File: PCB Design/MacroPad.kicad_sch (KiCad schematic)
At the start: 64 parts, among them J1 USB_C_Receptacle_USB2.0_16P, J2 Conn_01x03_Pin, SW1 SW_DPST, SW2 SW_DPST, U1 RP2040, U2 AMS1117-3.3, U3 W25Q128JVS, U4 SN74LV1T34DBV, Y1 ABM8-272-T3

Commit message: Add second sheet
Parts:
- added C25: 1uF, symbol Device:C_Small
- added R25: 100M, symbol Device:R_Small
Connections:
- net +5V: now also R25.1
- net GND: now also C25.1
- new net +5V_LED: C25.2, R25.2
- no-connect marks 4 -> 12
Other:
- added sheet Keys (MCU_&_Power.kicad_sch)
- note added: "RESET"
- note removed: "RESET BUTTON"
- moved on the sheet: C23, D5, D6, D7, R16, R17, R18, R19, R20, U4

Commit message: Refactor and layout page 1
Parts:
- C23: value C_Small -> 100nF
- U4: value SN74LV1T34DBV -> SN74LV1T34DBVR
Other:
- note added: "LED SIGNAL LEVEL SHIFTER"
- note added: "POWER FOR KEY LEDS"
- note removed: "LED LEVEL SHIFTER"
- moved on the sheet: C1, C10, C11, C12, C13, C14, C15, C16, C17, C18, C19, C2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

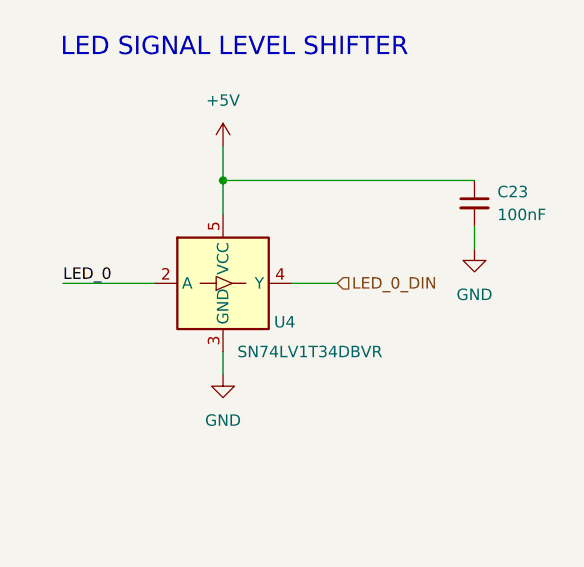
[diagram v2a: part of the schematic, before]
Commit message: Add underkey LEDs to schematic
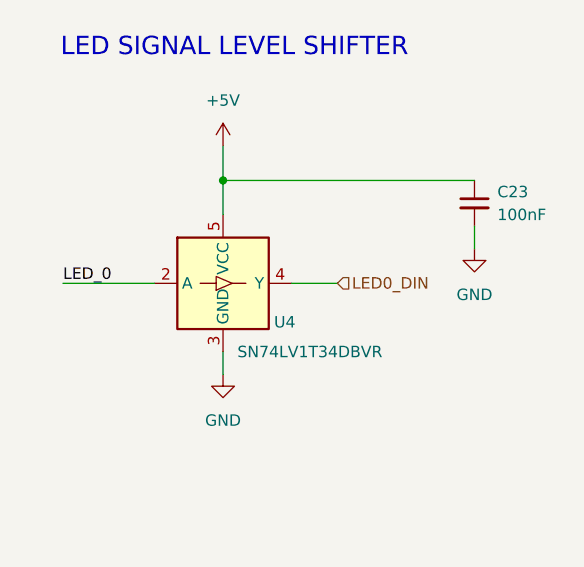
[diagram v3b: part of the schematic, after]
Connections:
- net LED_0_DIN renamed LED0_DIN
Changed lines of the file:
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@@
 		)
 	)
-	(hierarchical_label "LED_0_DIN"
+	(hierarchical_label "LED0_DIN"
 		(shape input)
 		(at 377.19 109.22 0)

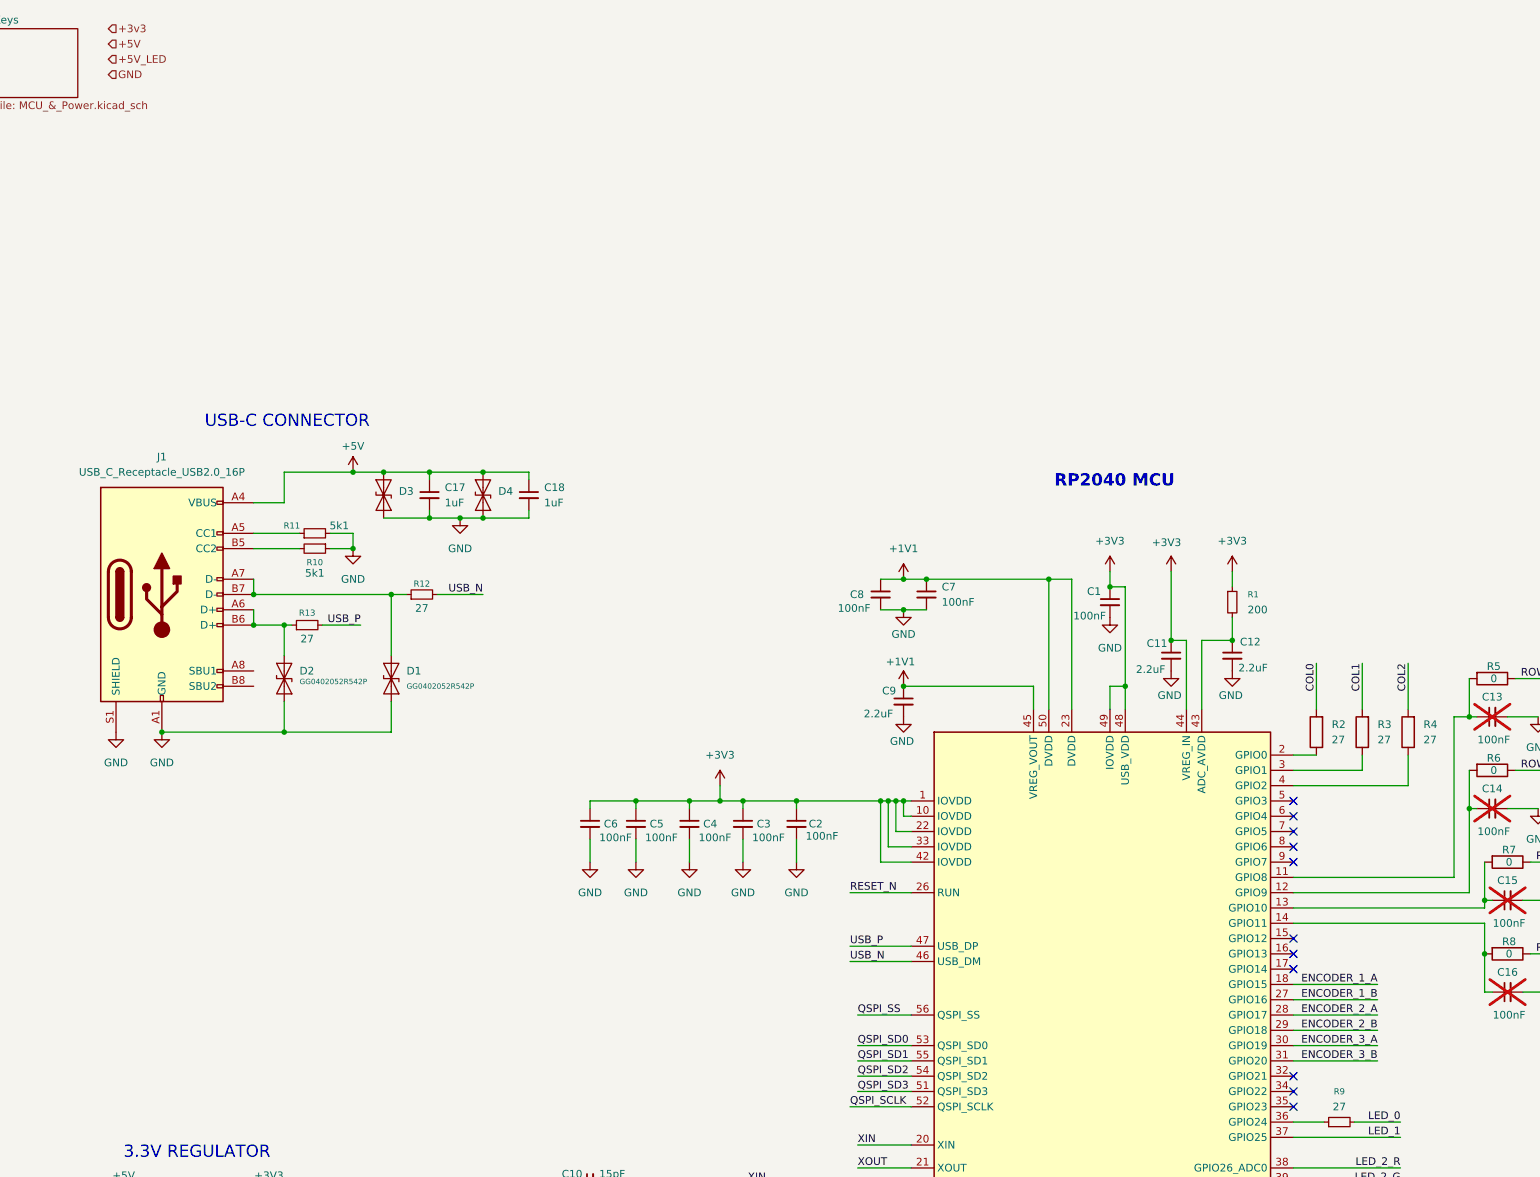
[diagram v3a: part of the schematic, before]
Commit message: Add mounting holes, fix some ERC errors
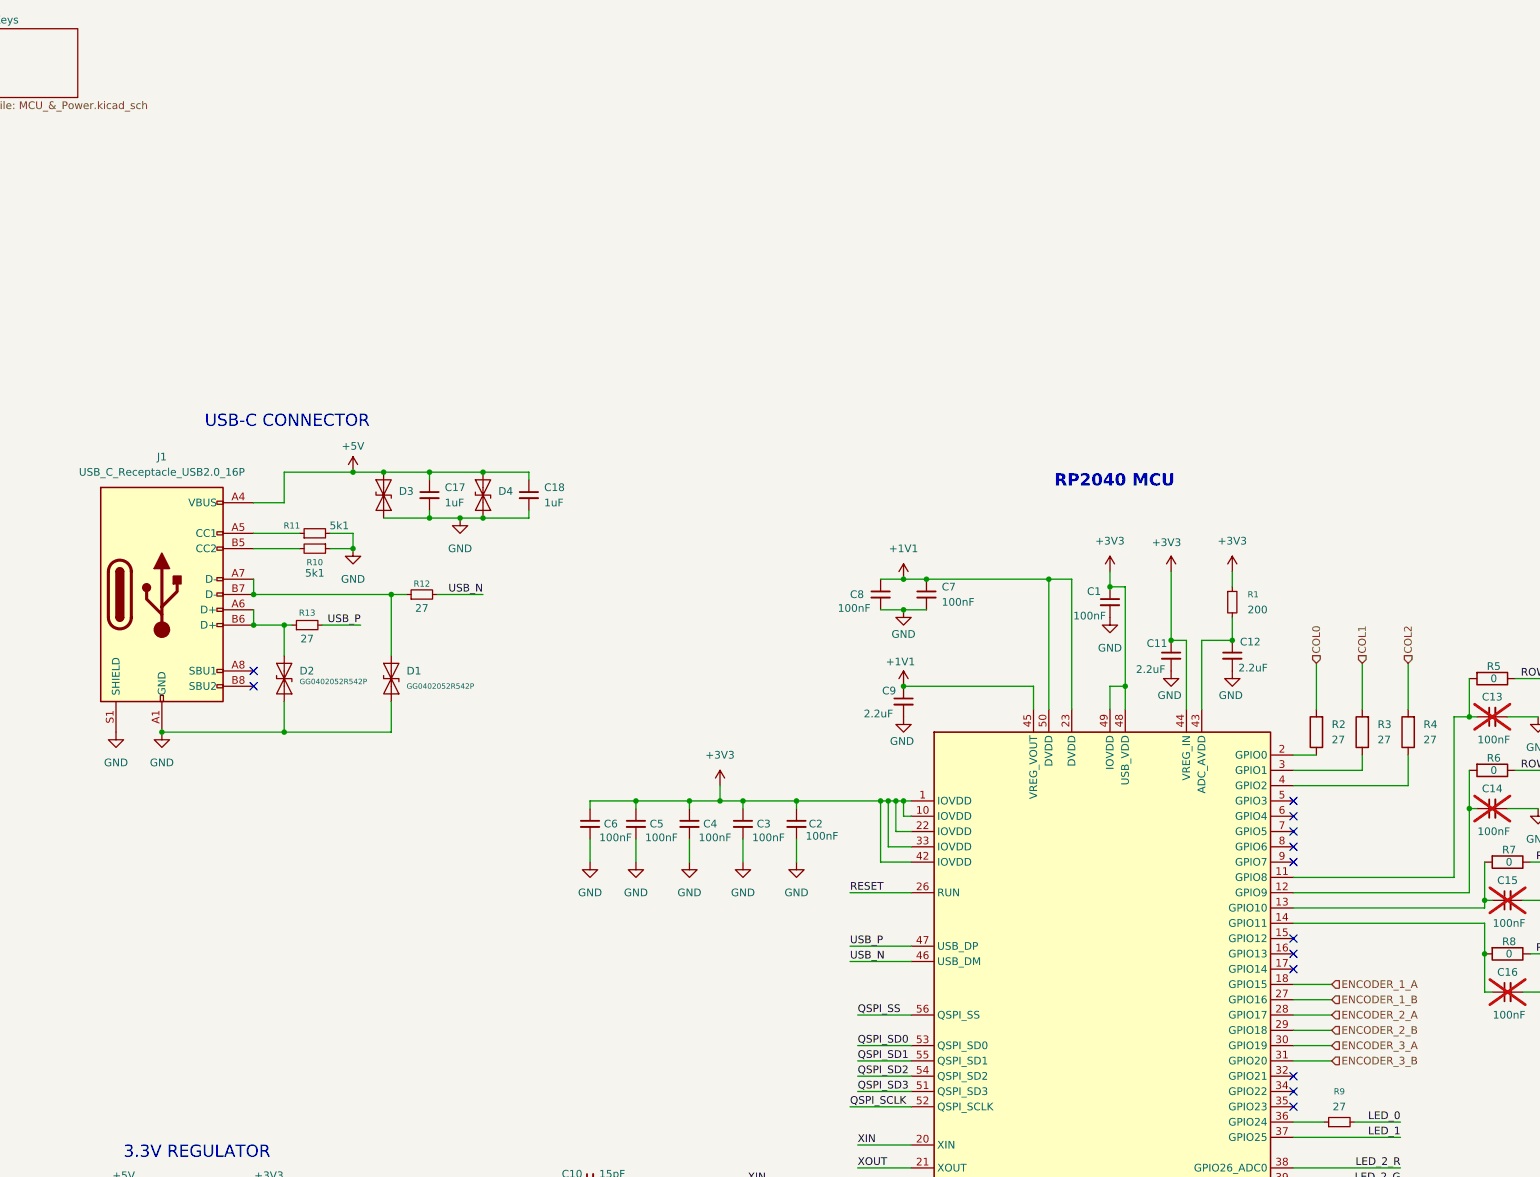
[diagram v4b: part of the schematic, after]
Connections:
- net RESET_N is gone; now on net RESET: U1.26 (RUN)
- no-connect marks 12 -> 14

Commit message: More ERC fixes
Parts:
- removed C25: 1uF, symbol Device:C_Small
- removed R25: 100M, symbol Device:R_Small
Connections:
- net +1V1: no longer names the net of C7.1, C8.1, C9.1, U1.23 (DVDD), U1.45 (VREG_VOUT), U1.50 (DVDD)
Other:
- note removed: "POWER FOR KEY LEDS"
- moved on the sheet: C1, C7, C8, C9

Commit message: Assign footprints
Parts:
- C1, C10, C11, C12, C13, C14, C15, C16, C17, C18, C19, C2, C20, C22, C23, C24, C3, C4, C5, C6, C7, C8, C9: footprint (none) -> Capacitor_SMD:C_0402_1005Metric
- C21: footprint (none) -> Capacitor_SMD:C_1206_3216Metric
- D7: footprint (none) -> LED_SMD:LED_Kingbright_APHBM2012_2x1.25mm
- J1: footprint (none) -> Connector_USB:USB_C_Receptacle_Amphenol_12401548E4-2A
- R1, R10, R11, R12, R13, R14, R16, R17, R18, R19, R2, R20, R21, R22, R23, R24, R3, R4, R5, R6, R7, R8, R9: footprint (none) -> Resistor_SMD:R_0402_1005Metric
- SW1, SW2: footprint (none) -> Button_Switch_SMD:SW_SPST_Omron_B3FS-101xP
- Y1: footprint (none) -> Crystal:Crystal_SMD_Abracon_ABM8G-4Pin_3.2x2.5mm

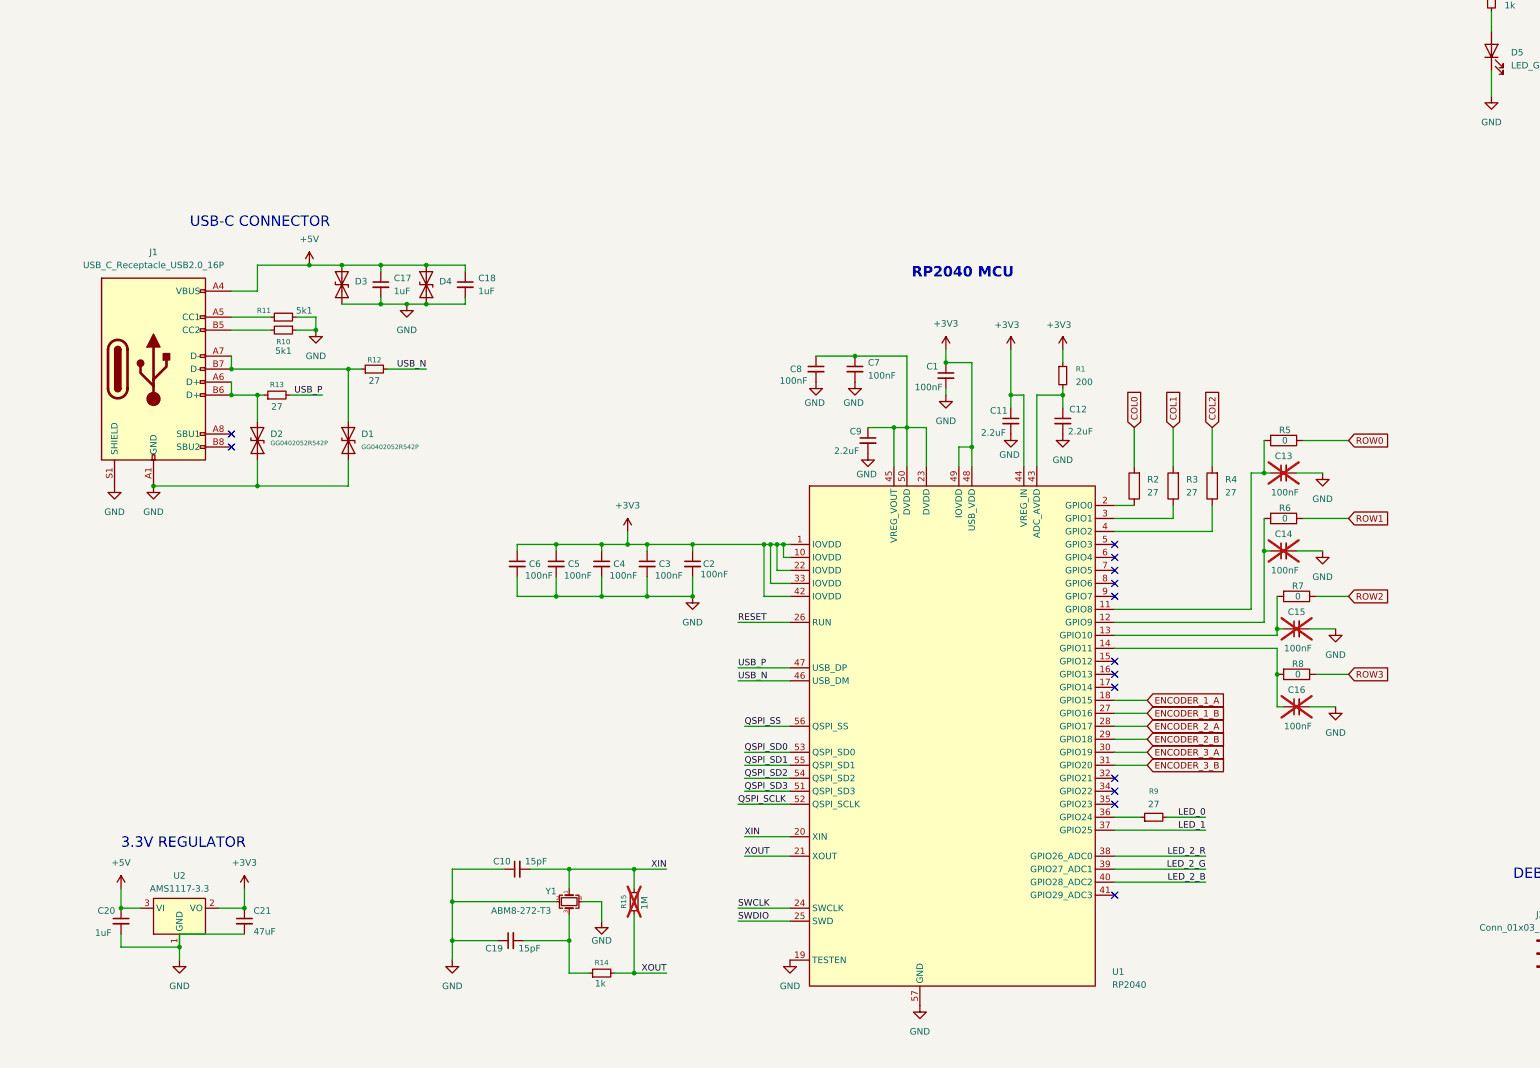
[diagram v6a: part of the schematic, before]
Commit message: More footprints.
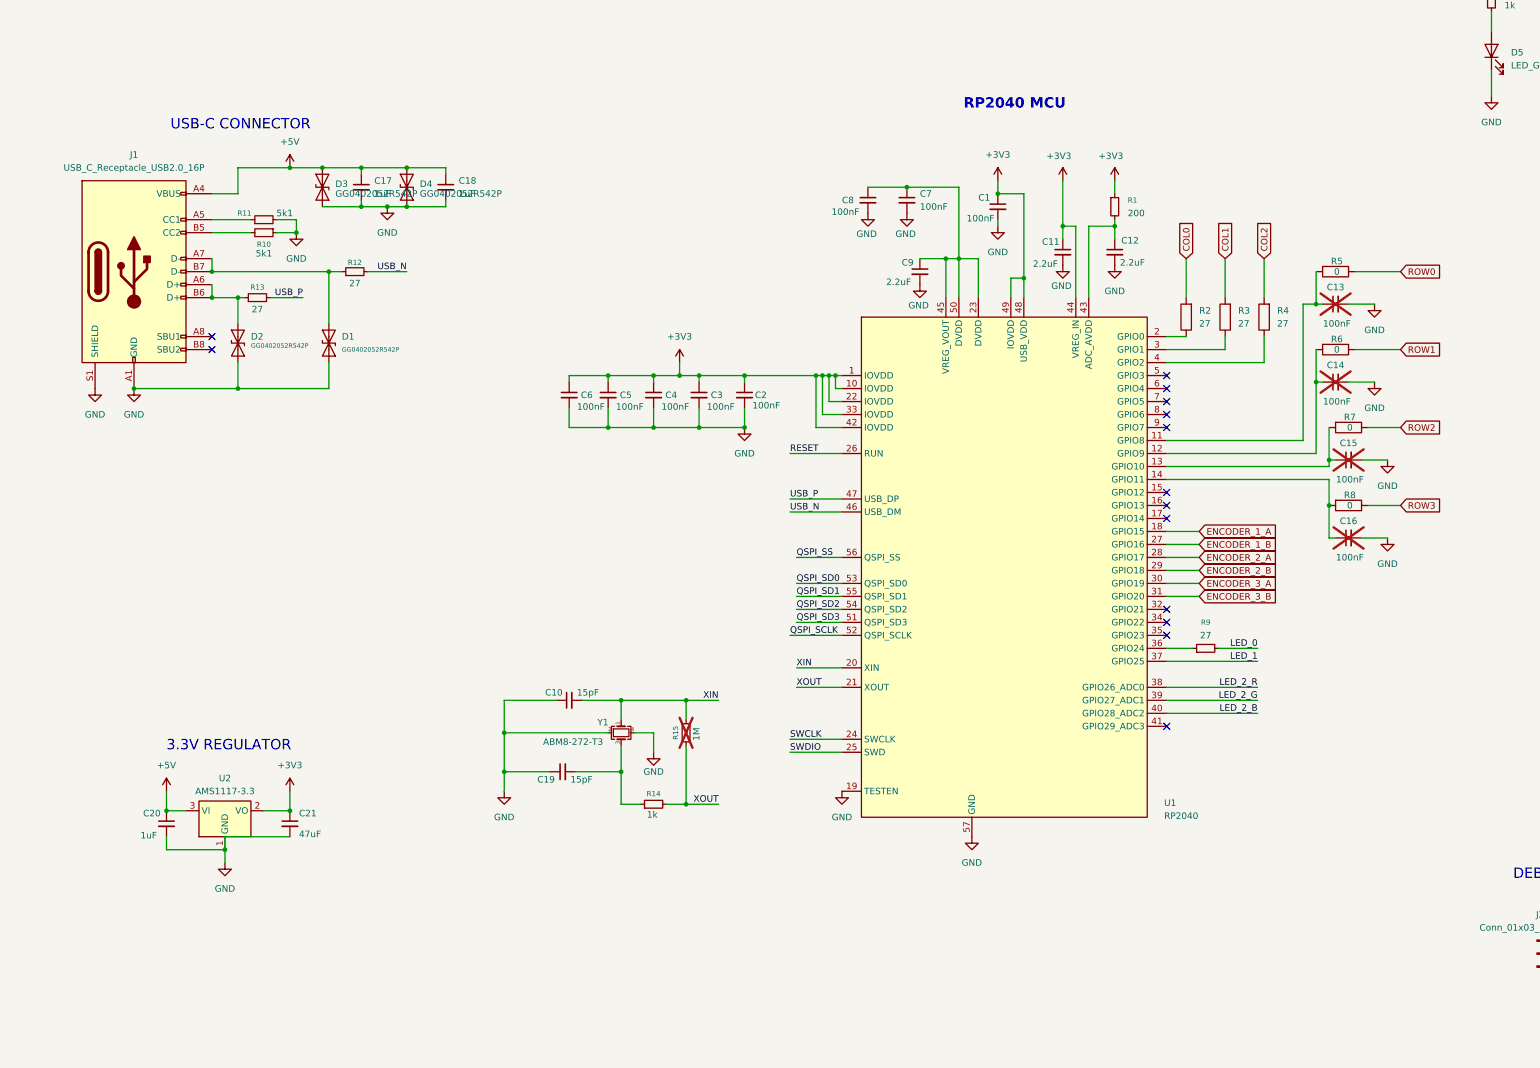
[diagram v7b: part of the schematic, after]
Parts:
- D1, D2: footprint Diode_SMD:D_SMA -> Diode_SMD:D_0402_1005Metric
- D3, D4: value ~ -> GG0402052R542P; footprint Diode_SMD:D_SMA -> Diode_SMD:D_0402_1005Metric
- D5, D6: footprint (none) -> LED_SMD:LED_0805_2012Metric
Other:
- title: (none) -> MacroPad
- moved on the sheet: C1, C10, C11, C12, C13, C14, C15, C16, C17, C18, C19, C2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
